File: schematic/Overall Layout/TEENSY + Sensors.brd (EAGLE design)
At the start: 54.6 x 68.2 mm, 15 parts, among them M7 SERVO, M8 SERVO, M9 SERVO, U1 MAX13054ASA, U6 55DEG, U7 55DEG

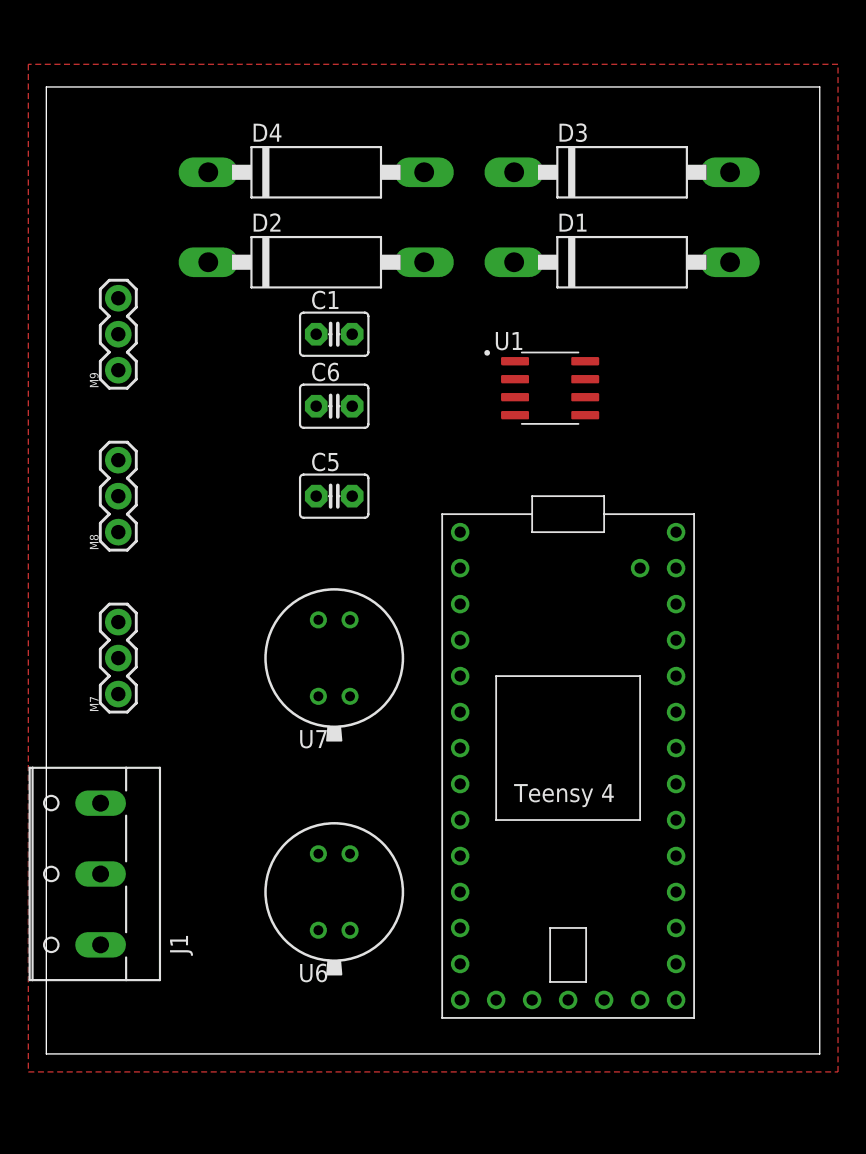
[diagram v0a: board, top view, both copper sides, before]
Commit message: Added military connectors to CAN Bus and added copper threading to PCB designs
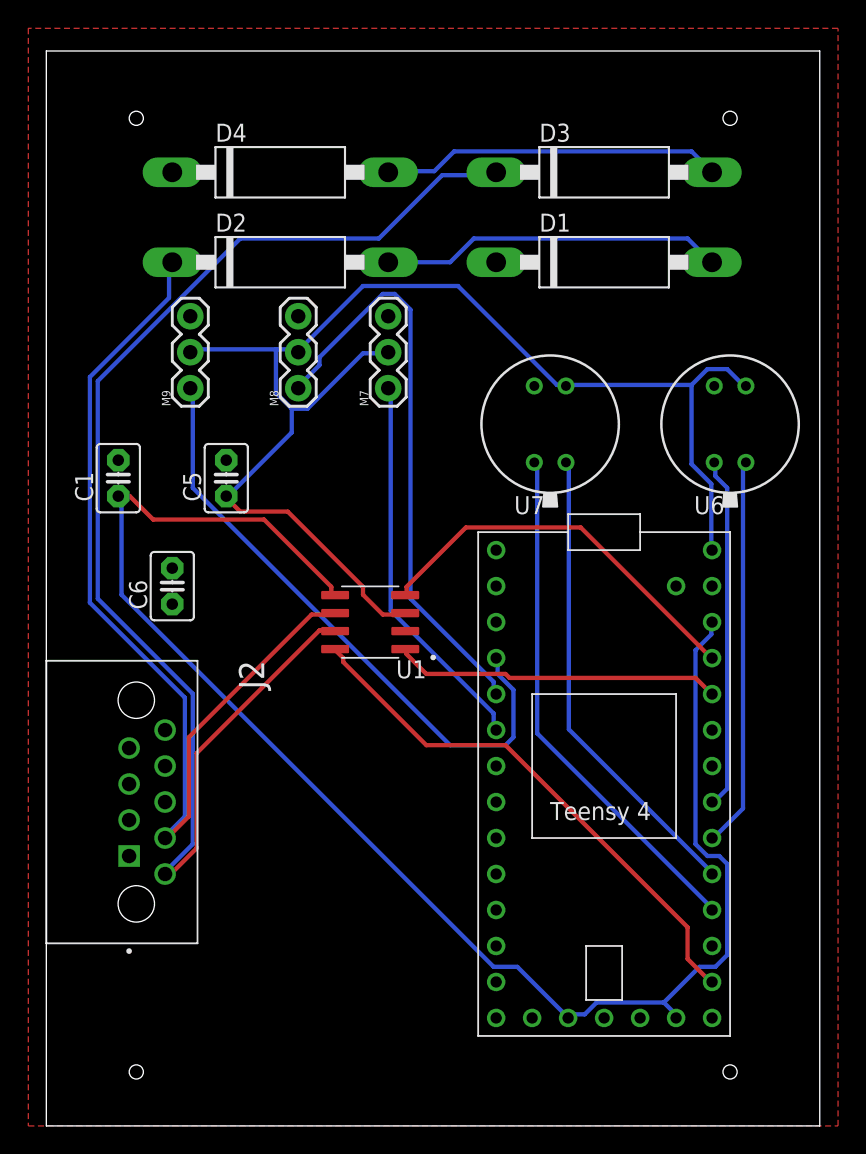
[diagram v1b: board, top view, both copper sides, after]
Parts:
- removed J1: (no value), con-wago-500:W237-103
- added J2: M83513/10-A01NP, M83513_10-A01NP:BEL_M83513/10-A01NP
- moved U6 43.3 mm to (48.3, 44.5)
- moved M7 28.8 mm to (24.1, 47.0)
- moved U7 22.5 mm to (35.6, 44.5)
- moved U1 20.8 mm to (22.9, 30.5), turned to 180 degrees
- moved C1 18.3 mm to (5.08, 40.6), turned to 90 degrees
- moved C6 17.1 mm to (8.89, 33.0), turned to 90 degrees
- moved M8 16.3 mm to (17.8, 47.0)
- moved C5 7.73 mm to (12.7, 40.6), turned to 90 degrees
- moved M9 5.24 mm to (10.2, 47.0)
- moved U$2 2.84 mm to (39.4, 20.3)
- moved D2 2.54 mm to (16.5, 55.9)
- moved D4 2.54 mm to (16.5, 62.2)
- moved D1 1.27 mm to (39.4, 55.9)
- moved D3 1.27 mm to (39.4, 62.2)
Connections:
- net CAN_BUS: now also J2.6; no longer J1.1
- net GND: now also J2.8; no longer J1.3
- net N$5: now also J2.7; no longer J1.2
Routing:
- net +3V3: track 0.00 -> 109.5 mm
- net CAN_BUS: track 0.00 -> 95.8 mm
- net VCC: track 0.00 -> 95.5 mm
- net N$5: track 0.00 -> 68.6 mm
- net N$52: track 0.00 -> 43.7 mm
- net N$51: track 0.00 -> 41.2 mm
- net N$46: track 0.00 -> 37.9 mm
- net N$49: track 0.00 -> 36.8 mm
- net N$48: track 0.00 -> 33.3 mm
- net N$1: track 0.00 -> 27.8 mm
- net N$55: track 0.00 -> 27.6 mm
- net N$50: track 0.00 -> 27.4 mm
- net N$53: track 0.00 -> 24.8 mm
- net N$4: track 0.00 -> 24.2 mm
- net N$7: track 0.00 -> 24.1 mm
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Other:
- board size 54.6 x 68.2 mm -> 54.6 x 75.9 mm
